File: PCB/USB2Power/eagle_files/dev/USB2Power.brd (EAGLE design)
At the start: 12.5 x 16.5 mm, 7 parts, among them SW1 PCM12SMTR

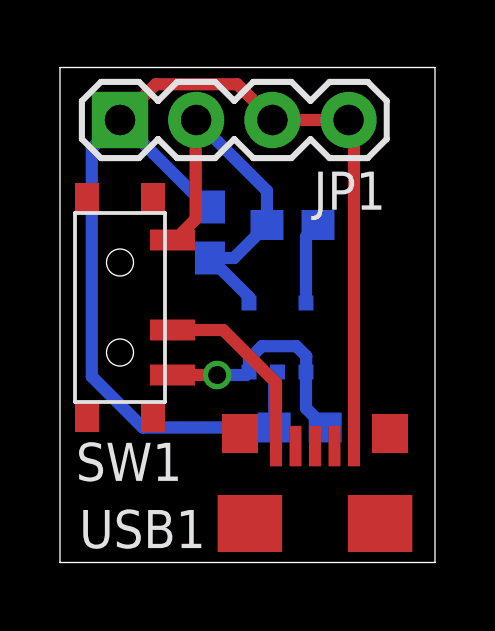
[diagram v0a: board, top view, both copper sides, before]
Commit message: Resolve DRC conflicts with USB2Power.brd
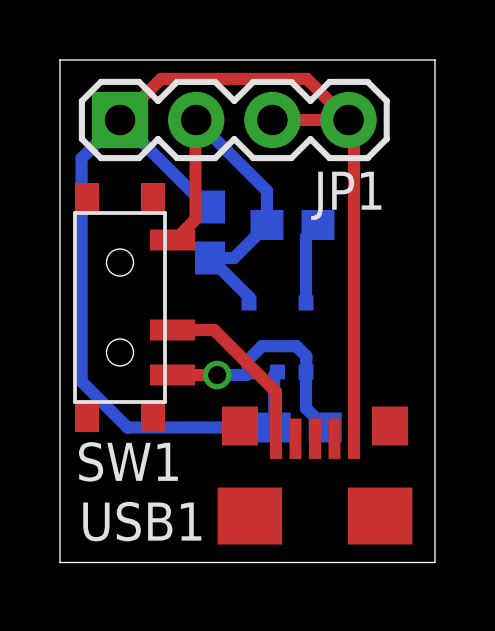
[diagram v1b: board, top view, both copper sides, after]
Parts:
- moved USB1 0.25 mm to (8.50, 2.50)
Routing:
- net GND: track 41.4 -> 44.4 mm
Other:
- board size 12.5 x 16.5 mm -> 12.5 x 16.8 mm
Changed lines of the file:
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@@
 <plain>
 <wire x1="0" y1="0" x2="12.5" y2="0" width="0" layer="20"/>
-<wire x1="12.5" y1="0" x2="12.5" y2="16.5" width="0" layer="20"/>
-<wire x1="12.5" y1="16.5" x2="0" y2="16.5" width="0" layer="20"/>
-<wire x1="0" y1="16.5" x2="0" y2="0" width="0" layer="20"/>
+<wire x1="12.5" y1="0" x2="12.5" y2="16.75" width="0" layer="20"/>
+<wire x1="12.5" y1="16.75" x2="0" y2="16.75" width="0" layer="20"/>
+<wire x1="0" y1="16.75" x2="0" y2="0" width="0" layer="20"/>
 </plain>
 <attributes>
@@
 <attribute name="NAME" x="0.53" y="2.72" size="1.27" layer="25"/>
 </element>
-<element name="USB1" library="freddyLibr" package="USB-MICROB-SMT" value="USB-MICROB-SMT5-PIN" x="8.5" y="2.25" smashed="yes">
-<attribute name="NAME" x="0.64" y="0.48" size="1.27" layer="25"/>
+<element name="USB1" library="freddyLibr" package="USB-MICROB-SMT" value="USB-MICROB-SMT5-PIN" x="8.5" y="2.5" smashed="yes">
+<attribute name="NAME" x="0.64" y="0.73" size="1.27" layer="25"/>
 </element>
 <element name="VR1" library="freddyLibr" package="UJ-5_TSOT" value="" x="7.25" y="7.5" smashed="yes" rot="MR0">
@@
 <contactref element="JP1" pad="4"/>
 <contactref element="JP1" pad="3"/>
-<wire x1="9.8" y1="3.88" x2="9.8" y2="14.57" width="0.4064" layer="1"/>
-<wire x1="9.8" y1="14.57" x2="9.62" y2="14.75" width="0.4064" layer="1"/>
-<wire x1="9.62" y1="14.75" x2="7.08" y2="14.75" width="0.4064" layer="1"/>
-<wire x1="7.08" y1="14.75" x2="7.08" y2="14.77" width="0.4064" layer="1"/>
-<wire x1="7.08" y1="14.77" x2="5.91" y2="15.94" width="0.4064" layer="1"/>
-<wire x1="5.91" y1="15.94" x2="3.19" y2="15.94" width="0.4064" layer="1"/>
-<wire x1="3.19" y1="15.94" x2="2" y2="14.75" width="0.4064" layer="1"/>
 <wire x1="7.14" y1="4.5" x2="7.14" y2="6.24" width="0.4064" layer="16"/>
 <wire x1="7.14" y1="6.24" x2="7.25" y2="6.35" width="0.4064" layer="16"/>
 <wire x1="5" y1="11.85" x2="4.9" y2="11.85" width="0.4064" layer="16"/>
 <wire x1="4.9" y1="11.85" x2="2" y2="14.75" width="0.4064" layer="16"/>
-<wire x1="7.14" y1="4.5" x2="2.76" y2="4.5" width="0.4064" layer="16"/>
-<wire x1="2.76" y1="4.5" x2="1.06" y2="6.2" width="0.4064" layer="16"/>
-<wire x1="1.06" y1="6.2" x2="1.06" y2="13.81" width="0.4064" layer="16"/>
-<wire x1="1.06" y1="13.81" x2="2" y2="14.75" width="0.4064" layer="16"/>
+<wire x1="7.14" y1="4.5" x2="2.25" y2="4.5" width="0.4064" layer="16"/>
+<wire x1="2.25" y1="4.5" x2="0.72" y2="6.03" width="0.4064" layer="16"/>
+<wire x1="0.72" y1="6.03" x2="0.72" y2="13.47" width="0.4064" layer="16"/>
+<wire x1="0.72" y1="13.47" x2="2" y2="14.75" width="0.4064" layer="16"/>
+<wire x1="9.62" y1="14.75" x2="9.6" y2="14.75" width="0.4064" layer="1"/>
+<wire x1="9.6" y1="14.75" x2="8.23" y2="16.12" width="0.4064" layer="1"/>
+<wire x1="8.23" y1="16.12" x2="3.37" y2="16.12" width="0.4064" layer="1"/>
+<wire x1="3.37" y1="16.12" x2="2" y2="14.75" width="0.4064" layer="1"/>
+<wire x1="7.08" y1="14.75" x2="9.62" y2="14.75" width="0.4064" layer="1"/>
+<wire x1="9.8" y1="4.13" x2="9.8" y2="14.57" width="0.4064" layer="1"/>
+<wire x1="9.8" y1="14.57" x2="9.62" y2="14.75" width="0.4064" layer="1"/>
 </signal>
 <signal name="VIN">
 <contactref element="USB1" pad="5"/>
 <contactref element="SW1" pad="2"/>
-<wire x1="7.2" y1="3.88" x2="7.2" y2="5.99" width="0.4064" layer="1"/>
-<wire x1="7.2" y1="5.99" x2="5.44" y2="7.75" width="0.4064" layer="1"/>
-<wire x1="5.44" y1="7.75" x2="3.75" y2="7.75" width="0.4064" layer="1"/>
+<wire x1="3.75" y1="7.75" x2="5.14" y2="7.75" width="0.4064" layer="1"/>
+<wire x1="5.14" y1="7.75" x2="7.2" y2="5.69" width="0.4064" layer="1"/>
+<wire x1="7.2" y1="5.69" x2="7.2" y2="4.13" width="0.4064" layer="1"/>
 </signal>
 <signal name="VOUT">
